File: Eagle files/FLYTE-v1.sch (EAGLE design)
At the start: 31 parts, among them J1 U.FL-R-SMT(01), Q2 IRLB8721PBF, U2 AMS1117-3.3, U3 CORE1262-868M, U4 NEO-6M-GPS, U5 M24C16-RMN6TP, X1 LTI-SASF54GT

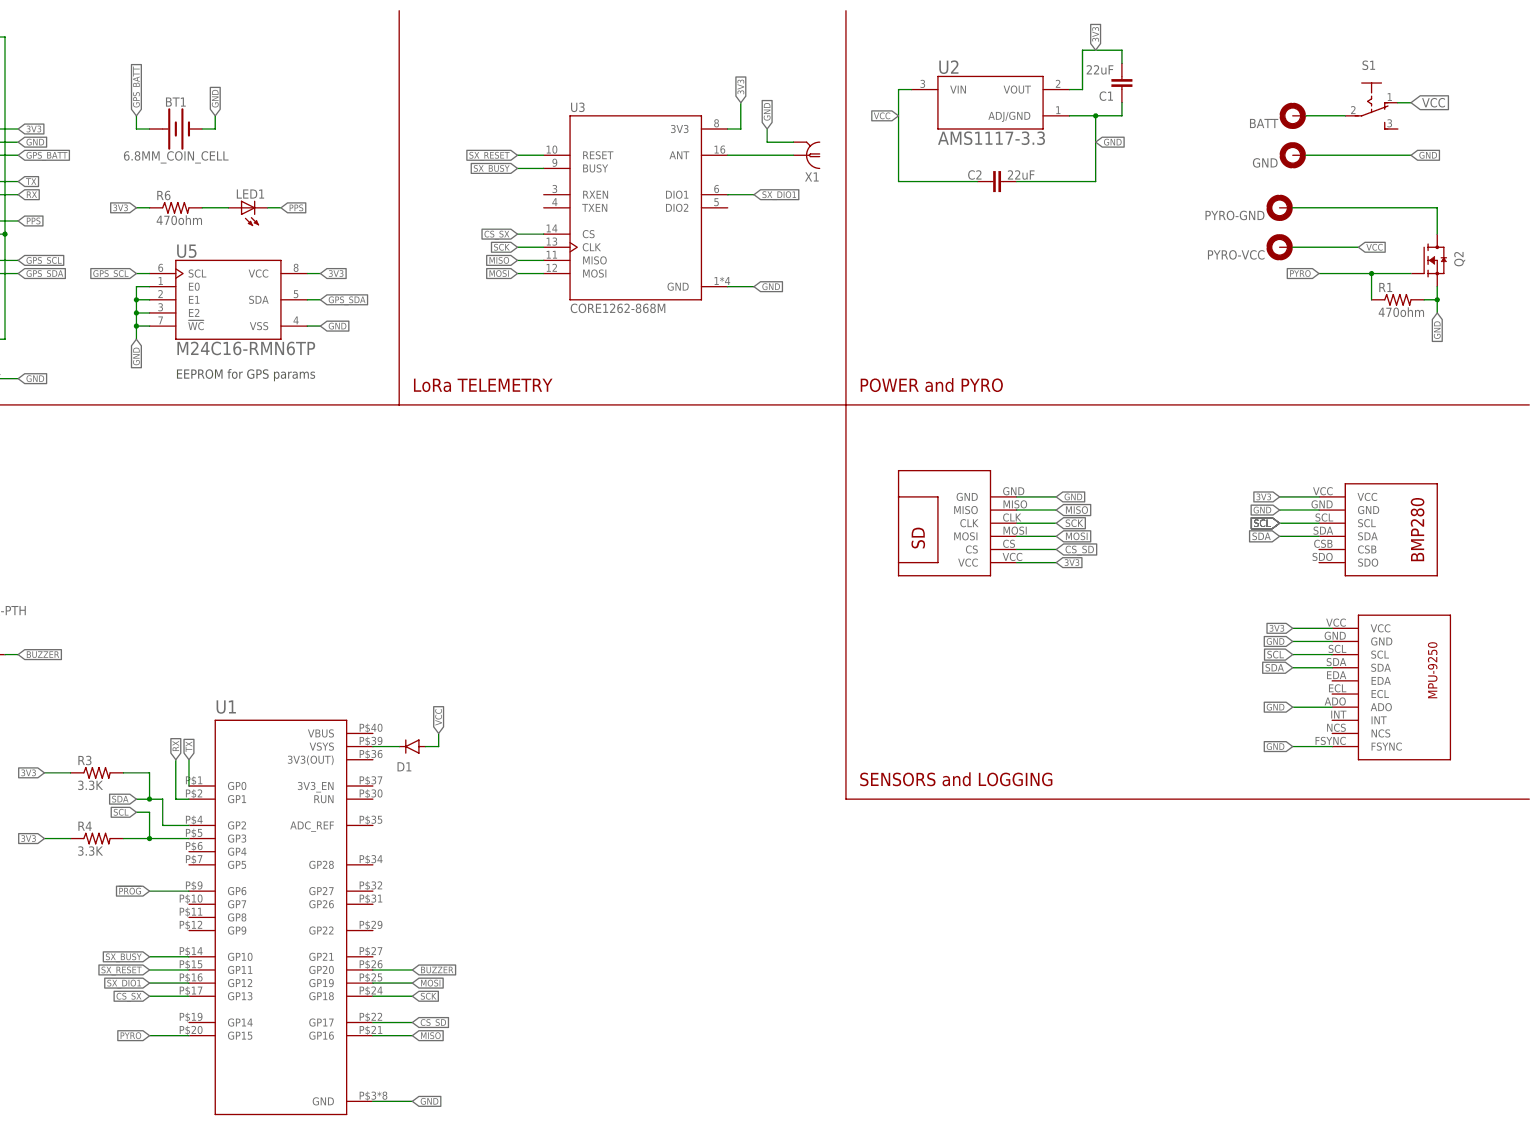
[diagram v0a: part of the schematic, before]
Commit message: Modify pyro and power section
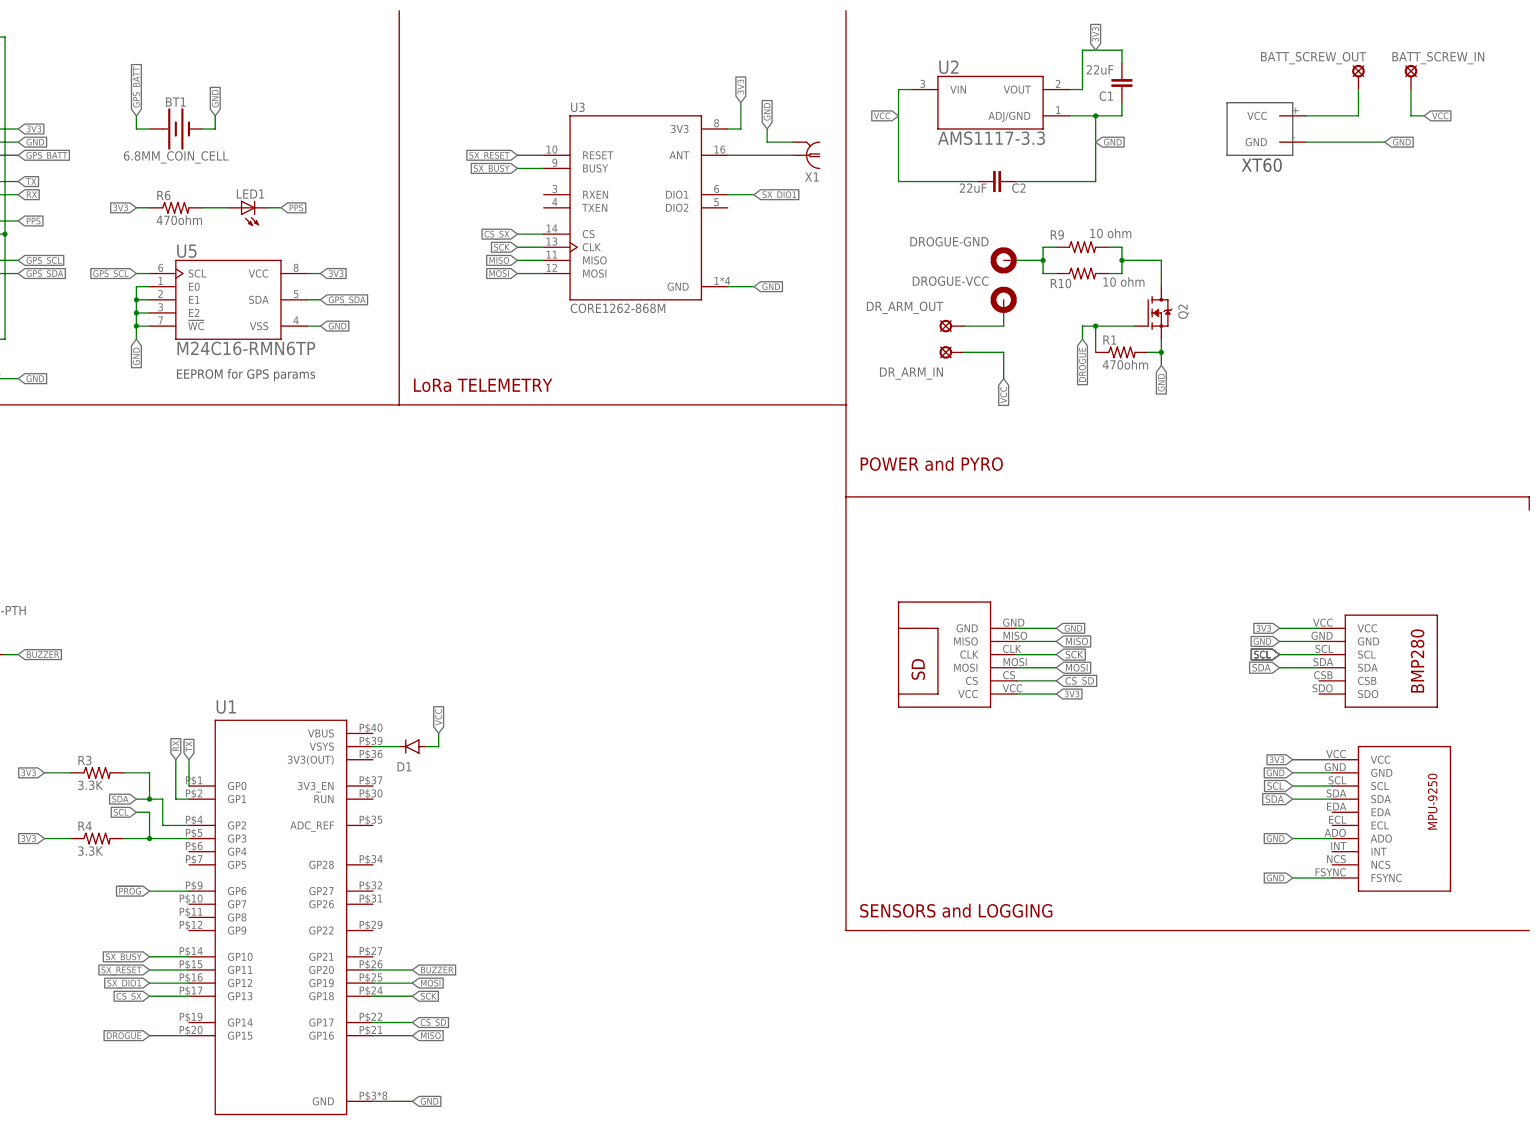
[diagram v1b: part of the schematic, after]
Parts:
- removed BATT, GND, PYRO-GND, PYRO-VCC: MOUNT-PAD-ROUND3.0, holes:MOUNT-PAD-ROUND3.0
- removed S1: (no value), switch:255SB
- added BATT_IN: XT60, XT60:XT60
- added BATT_SCREW_IN, BATT_SCREW_OUT, DR_ARM_IN, DR_ARM_OUT: LSP10, solpad:LSP10
- added DROGUE-GND, DROGUE-VCC: MOUNT-PAD-ROUND3.0, holes:MOUNT-PAD-ROUND3.0
- added R10, R9: 10 ohm, rcl:R-US_0207/10
- Q2: value IRLB8721PBF -> IRF540NPBF; device IRLB8721PBF:IRLB8721PBF -> IRF540NPBF:IRF540NPBF
- R1: device adafruit:R-US_R0805 -> rcl:R-US_R0805
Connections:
- net PYRO renamed DROGUE
- new net N$12: Q2.D, R10.2, R9.2
- new net N$7: DROGUE-GND.MOUNT, R10.1, R9.1
- net GND: now also BATT_IN.GND, C2.1; no longer C2.2, GND.MOUNT
- net N$3: now also BATT_IN.VCC, BATT_SCREW_OUT.MP; no longer BATT.MOUNT, S1.P
- net N$5: now also DROGUE-VCC.MOUNT, DR_ARM_OUT.MP; no longer PYRO-GND.MOUNT, Q2.D
- net VCC: now also BATT_SCREW_IN.MP, C2.2, DR_ARM_IN.MP; no longer C2.1, PYRO-VCC.MOUNT, S1.O
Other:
- moved on the sheet: C2, R1

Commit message: Finish chematic except gps
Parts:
- removed BT1: 6.8MM_COIN_CELL, SparkFun-Batteries:BATTERY-6.8MM_SMD
- removed J1: U.FL-R-SMT(01), U.FL-R-SMT_01_:U.FL-R-SMT(01)
- removed L1: 27uH, rcl:L-USL2012C
- removed LED1: (no value), adafruit:LEDCHIPLED_1206
- removed R5: 3.3K, adafruit:R-US_R0805
- removed R6: 470ohm, adafruit:R-US_R0805
- removed R7: 22ohm, adafruit:R-US_R0805
- removed S2: (no value), switch:320-916
- removed U4: NEO-6M-GPS, NEO-6M-GPS:NEO-6M-GPS
- removed U5: M24C16-RMN6TP, M24C16-RMN6TP:M24C16-RMN6TP
- removed X1: LTI-SASF54GT, con-coax:LTI-SASF54GT
- added J2: CONSMA002, CONSMA002:CONSMA002
- added MAIN-GND, MAIN-VCC: MOUNT-PAD-ROUND3.0, holes:MOUNT-PAD-ROUND3.0
- added MA_ARM_IN, MA_ARM_OUT: LSP10, solpad:LSP10
- added Q1: IRF540NPBF, IRF540NPBF:IRF540NPBF
- added R11, R12: 10 ohm, rcl:R-US_0207/10
- added R13, R14, R15, R18: 4.7K ohm, rcl:R-US_R0805
- added R16, R17: 100K ohm, rcl:R-US_R0805
- added R8: 470ohm, rcl:R-US_R0805
- added S1: MOMENTARY-SWITCH-SPST-PTH-6.0MM, SparkFun-Switches:MOMENTARY-SWITCH-SPST-PTH-6.0MM
- added SW1: 1825159-1, 1825159-1:1825159-1
- added U6: W25Q32JVSSIQ, W25Q32JVSSIQ:W25Q32JVSSIQ
- R2: device adafruit:R-US_R0805 -> rcl:R-US_R0805
- R3, R4: value 3.3K -> 3.3K ohm; device adafruit:R-US_R0805 -> rcl:R-US_R0805
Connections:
- removed net !PROG: R5.1, S2.P, U1.GP6
- removed net GPS_BATT: BT1.+, U4.V_BCKP
- removed net GPS_SCL: U4.SCL2, U5.SCL
- removed net GPS_SDA: U4.SDA2, U5.SDA
- removed net MISO: U$3.MISO, U1.GP16, U3.MISO
- removed net MOSI: U$3.MOSI, U1.GP19, U3.MOSI
- removed net N$10: J1.SIG, L1.2, U4.RF_IN
- removed net N$11: L1.1, R7.1
- removed net N$9: LED1.A, R6.2
- removed net PPS: LED1.C, U4.TIMEPULSE
- removed net SCK: U$3.CLK, U1.GP18, U3.CLK
- new net CS_FLASH: R15.2, U1.GP9, U6.!CS
- new net MAIN: Q1.G, R8.1, U1.GP14
- new net MISO_0: R16.1, U1.GP16, U3.MISO
- new net MISO_1: R17.2, U$3.MISO, U1.GP12, U6.DO(IO1)
- new net MOSI_0: U1.GP19, U3.MOSI
- new net MOSI_1: U$3.MOSI, U1.GP11, U6.DI(IO0)
- new net N$13: Q1.D, R11.2, R12.2
- new net N$14: MAIN-VCC.MOUNT, MA_ARM_OUT.MP
- new net N$6: MAIN-GND.MOUNT, R11.1, R12.1
- new net PROG: R18.2, SW1.2, U1.GP6
- new net SCK_0: U1.GP18, U3.CLK
- new net SCK_1: U$3.CLK, U1.GP10, U6.CLK
- new net SX_DIO2: U1.GP21, U3.DIO2
- net 3V3: now also R13.2, R14.1, R15.1, R16.2, R17.1, SW1.3, U6.!HOLD!/!RESET!(IO3), U6.!WP!(IO2), U6.VCC; no longer R5.2, R6.1, S2.O, U4.VCC, U5.VCC
- net BUZZER: now also R2.2; no longer R2.1
- net CS_SD: now also R14.2, U1.GP13; no longer U1.GP17
- net CS_SX: now also R13.1, U1.GP17; no longer U1.GP13
- net GND: now also J2.2, Q1.S, R18.1, R8.2, S1.2, SW1.1, U6.GND; no longer BT1.-, J1.GND, S2.S, U4.GND, U4.VDDUSB, U5.!WC, U5.E0, U5.E1, U5.E2, U5.VSS, X1.2
- net N$2: now also R2.1; no longer R2.2
- net N$4: now also J2.1; no longer X1.1
- net N$8: now also S1.1, U1.RUN; no longer R7.2, U4.RSVD_8, U4.VCC_RF
- net RX: no longer U4.TXD1
- net SX_BUSY: now also U1.GP27; no longer U1.GP10
- net SX_DIO1: now also U1.GP22; no longer U1.GP12
- net SX_RESET: now also U1.GP26; no longer U1.GP11
- net TX: no longer U4.RXD1
- net VCC: now also MA_ARM_IN.MP
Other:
- note added: "All CS lines have a pullup resistor to initialize all components as inactive If this is not done, garbage values may cause trouble Similarly, all MISO lines are pulled up as they are only used when slave components are in use. They might float otherwise"
- note added: "Data logging components communicate with pico on SPI1 bus"
- note added: "Telemetry communicates with pico on SPI0 bus"
- note removed: "EEPROM for GPS params"
- moved on the sheet: D1, LS1, R2, R3, R4, U1, U3

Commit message: Finish v1 schematic
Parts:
- added U$4: NEO-6M, NEO-6M:NEO-6M
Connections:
- net 3V3: now also U$4.VCC
- net GND: now also U$4.GND
- net RX: now also U$4.TX
- net TX: now also U$4.RX
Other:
- note added: "Push button to reset pico"
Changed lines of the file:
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@@
 <part name="R2" library="rcl" library_urn="urn:adsk.eagle:library:334" deviceset="R-US_" device="R0805" package3d_urn="urn:adsk.eagle:package:23553/2" value="470ohm"/>
 <part name="S1" library="SparkFun-Switches" deviceset="MOMENTARY-SWITCH-SPST" device="-PTH-6.0MM" override_package3d_urn="urn:adsk.eagle:package:40381829/2" override_package_urn="urn:adsk.eagle:footprint:40381830/1"/>
+<part name="U$4" library="NEO-6M" deviceset="NEO-6M" device="" override_package3d_urn="urn:adsk.eagle:package:40381906/2" override_package_urn="urn:adsk.eagle:footprint:40381907/1"/>
 </parts>
 <sheets>
@@
 Similarly, all MISO lines are pulled up as they are only used when slave
 components are in use. They might float otherwise</text>
+<text x="205.74" y="104.14" size="1.778" layer="97">Push button to reset pico</text>
 </plain>
 <instances>
@@
 <attribute name="NAME" x="187.96" y="105.664" size="1.778" layer="95" font="vector" align="bottom-center"/>
 </instance>
+<instance part="U$4" gate="G$1" x="71.12" y="215.9" smashed="yes"/>
 </instances>
 <busses>
@@
 <label x="195.58" y="104.14" size="1.27" layer="95" xref="yes"/>
 </segment>
+<segment>
+<wire x1="73.66" y1="210.82" x2="73.66" y2="205.74" width="0.1524" layer="91"/>
+<label x="73.66" y="205.74" size="1.27" layer="95" rot="R270" xref="yes"/>
+<pinref part="U$4" gate="G$1" pin="GND"/>
+</segment>
 </net>
 <net name="VCC" class="0">
@@
 <label x="83.82" y="86.36" size="1.27" layer="95" rot="R270" xref="yes"/>
 </segment>
+<segment>
+<wire x1="81.28" y1="210.82" x2="81.28" y2="205.74" width="0.1524" layer="91"/>
+<label x="81.28" y="205.74" size="1.27" layer="95" rot="R270" xref="yes"/>
+<pinref part="U$4" gate="G$1" pin="VCC"/>
+</segment>
 </net>
 <net name="TX" class="0">
@@
 <label x="142.24" y="111.76" size="1.27" layer="95" rot="R90" xref="yes"/>
 <pinref part="U1" gate="G$1" pin="GP0"/>
+</segment>
+<segment>
+<wire x1="78.74" y1="210.82" x2="78.74" y2="205.74" width="0.1524" layer="91"/>
+<label x="78.74" y="205.74" size="1.27" layer="95" rot="R270" xref="yes"/>
+<pinref part="U$4" gate="G$1" pin="RX"/>
 </segment>
 </net>
@@
 <pinref part="U1" gate="G$1" pin="GP1"/>
 </segment>
-</net>
+<segment>
+<wire x1="76.2" y1="210.82" x2="76.2" y2="205.74" width="0.1524" layer="91"/>
+<label x="76.2" y="205.74" size="1.27" layer="95" rot="R270" xref="yes"/>
+<pinref part="U$4" gate="G$1" pin="TX"/>
+</segment>
+</net>

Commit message: Finish layout
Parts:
- removed R2: 470ohm, rcl:R-US_R0805
- added C3, C4: 22uF, SparkFun-Capacitors:22UF-0805-6.3V-20%
- added JP1, JP2, JP3, JP4: (no value), adafruit:PINHD-1X3
- added U4: AMS1117-3.3, AMS1117-3.3:AMS1117-3.3
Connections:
- removed net N$2: LS1.2, R2.1
- new net 5V: C3.2, JP1.2, JP2.2, JP3.2, JP4.2, U4.VOUT
- new net SERVO1: JP1.1, U1.GP4
- new net SERVO2: JP2.1, U1.GP5
- new net SERVO3: JP3.1, U1.GP7
- new net SERVO4: JP4.1, U1.GP8
- net BUZZER: now also LS1.2; no longer R2.2
- net GND: now also C3.1, C4.1, JP1.3, JP2.3, JP3.3, JP4.3, U4.ADJ/GND
- net VCC: now also C4.2, U4.VIN
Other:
- moved on the sheet: R3, R4, U6

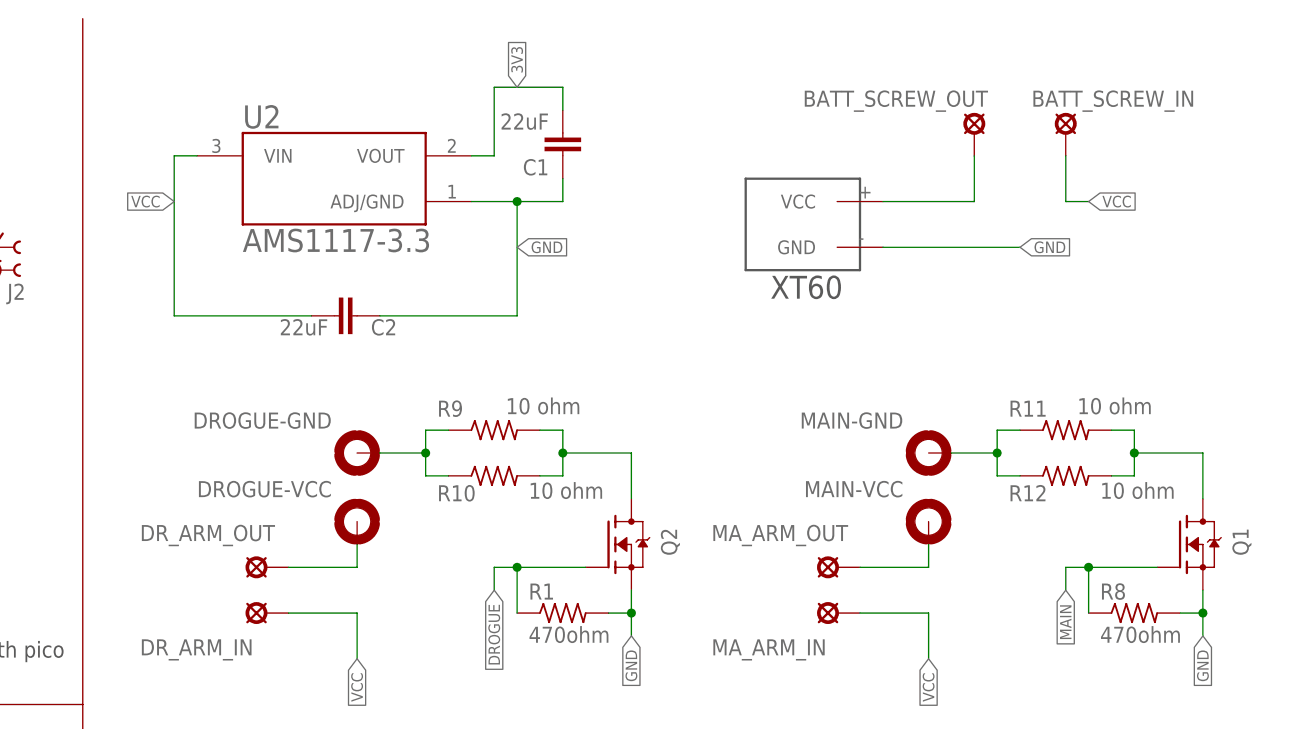
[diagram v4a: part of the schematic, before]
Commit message: Finish layout with GPS
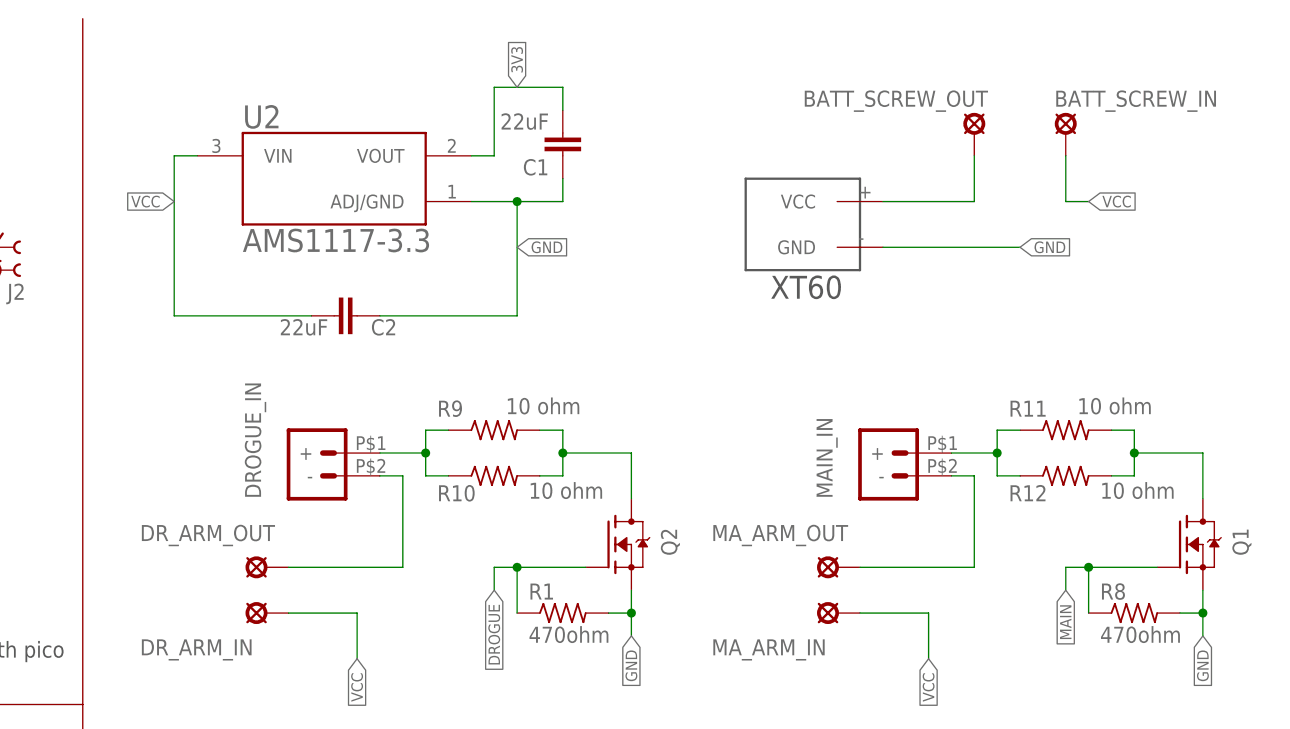
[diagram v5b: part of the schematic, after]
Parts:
- removed DROGUE-GND, DROGUE-VCC, MAIN-GND, MAIN-VCC: MOUNT-PAD-ROUND3.0, holes:MOUNT-PAD-ROUND3.0
- added DROGUE_IN, MAIN_IN: XT30UPB-M, XT30UPB-M:XT30UPB-M
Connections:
- removed net N$5: DROGUE-VCC.MOUNT, DR_ARM_OUT.MP
- new net N$2: DROGUE_IN.-, DR_ARM_OUT.MP
- net N$14: now also MAIN_IN.-; no longer MAIN-VCC.MOUNT
- net N$6: now also MAIN_IN.+; no longer MAIN-GND.MOUNT
- net N$7: now also DROGUE_IN.+; no longer DROGUE-GND.MOUNT

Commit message: move resistors, remove 1 screw sw
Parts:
- removed BATT_SCREW_IN, BATT_SCREW_OUT: LSP10, solpad:LSP10
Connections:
- removed net N$3: BATT_IN.VCC, BATT_SCREW_OUT.MP
- net VCC: now also BATT_IN.VCC; no longer BATT_SCREW_IN.MP
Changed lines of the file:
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@@
 <part name="MA_ARM_OUT" library="solpad" library_urn="urn:adsk.eagle:library:364" deviceset="LSP10" device="" package3d_urn="urn:adsk.eagle:package:26501/1" override_package3d_urn="urn:adsk.eagle:package:40384127/2" override_package_urn="urn:adsk.eagle:footprint:26494/1"/>
 <part name="MA_ARM_IN" library="solpad" library_urn="urn:adsk.eagle:library:364" deviceset="LSP10" device="" package3d_urn="urn:adsk.eagle:package:26501/1" override_package3d_urn="urn:adsk.eagle:package:40384127/2" override_package_urn="urn:adsk.eagle:footprint:26494/1"/>
-<part name="BATT_SCREW_OUT" library="solpad" library_urn="urn:adsk.eagle:library:364" deviceset="LSP10" device="" package3d_urn="urn:adsk.eagle:package:26501/1" override_package3d_urn="urn:adsk.eagle:package:40384127/2" override_package_urn="urn:adsk.eagle:footprint:26494/1"/>
-<part name="BATT_SCREW_IN" library="solpad" library_urn="urn:adsk.eagle:library:364" deviceset="LSP10" device="" package3d_urn="urn:adsk.eagle:package:26501/1" override_package3d_urn="urn:adsk.eagle:package:40384127/2" override_package_urn="urn:adsk.eagle:footprint:26494/1"/>
 </parts>
 <sheets>
@@
 <attribute name="NAME" x="321.31" y="185.801" size="1.778" layer="95"/>
 </instance>
-<instance part="BATT_SCREW_OUT" gate="1" x="350.52" y="243.84" smashed="yes">
-<attribute name="NAME" x="331.47" y="246.761" size="1.778" layer="95"/>
-</instance>
-<instance part="BATT_SCREW_IN" gate="1" x="360.68" y="243.84" smashed="yes">
-<attribute name="NAME" x="359.41" y="246.761" size="1.778" layer="95"/>
-</instance>
 </instances>
 <busses>
@@
 </segment>
 <segment>
-<wire x1="360.68" y1="236.22" x2="363.22" y2="236.22" width="0.1524" layer="91"/>
 <label x="363.22" y="236.22" size="1.27" layer="95" xref="yes"/>
-<wire x1="360.68" y1="241.3" x2="360.68" y2="236.22" width="0.1524" layer="91"/>
-<pinref part="BATT_SCREW_IN" gate="1" pin="MP"/>
+<pinref part="BATT_IN" gate="G$1" pin="VCC"/>
+<wire x1="363.22" y1="236.22" x2="340.36" y2="236.22" width="0.1524" layer="91"/>
 </segment>
 <segment>
@@
 </segment>
 </net>
-<net name="N$3" class="0">
-<segment>
-<wire x1="340.36" y1="236.22" x2="350.52" y2="236.22" width="0.1524" layer="91"/>
-<pinref part="BATT_IN" gate="G$1" pin="VCC"/>
-<wire x1="350.52" y1="241.3" x2="350.52" y2="236.22" width="0.1524" layer="91"/>
-<pinref part="BATT_SCREW_OUT" gate="1" pin="MP"/>
-</segment>
-</net>
